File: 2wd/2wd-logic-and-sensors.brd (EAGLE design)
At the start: 100 x 80 mm, 12 parts, among them IC1 REG1118

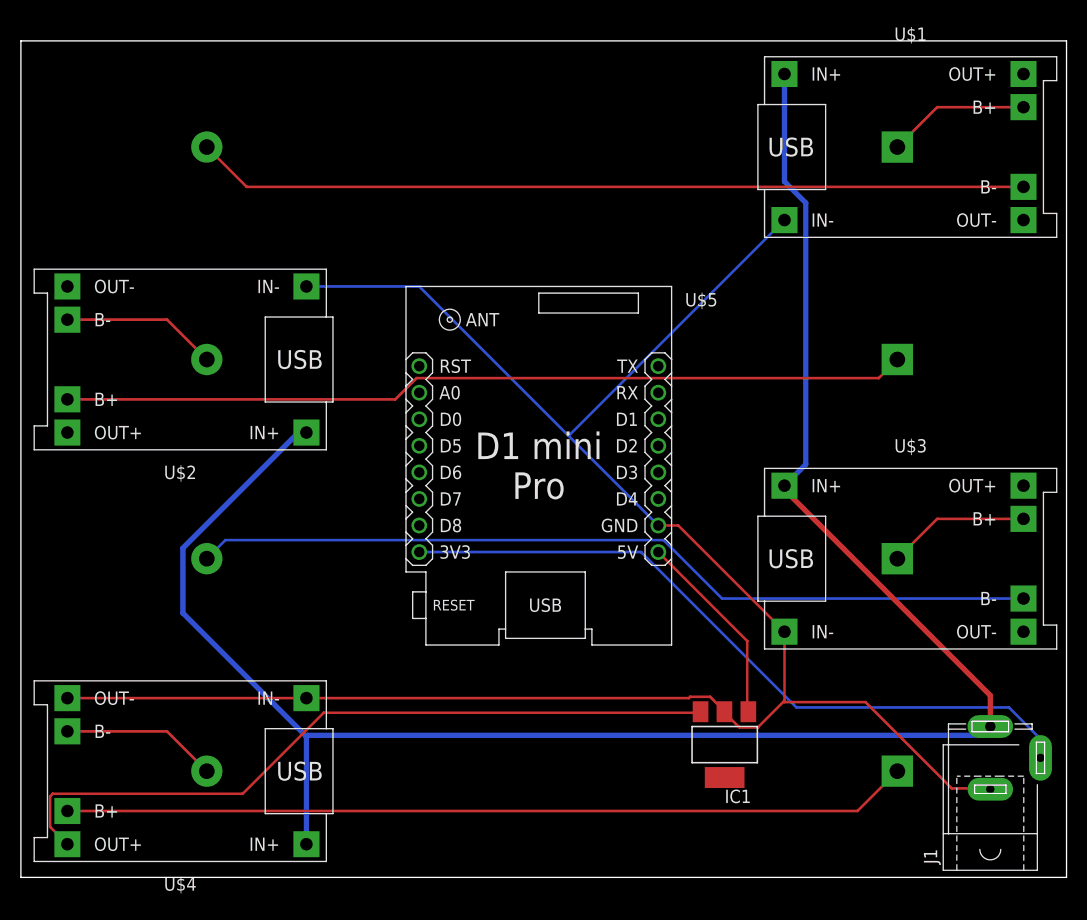
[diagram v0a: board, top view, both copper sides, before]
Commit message: Created two boards in Eagle.
Finally decided to create two boards within one Eagle project.  A motherboard and a power management/motor controller daughterboard.
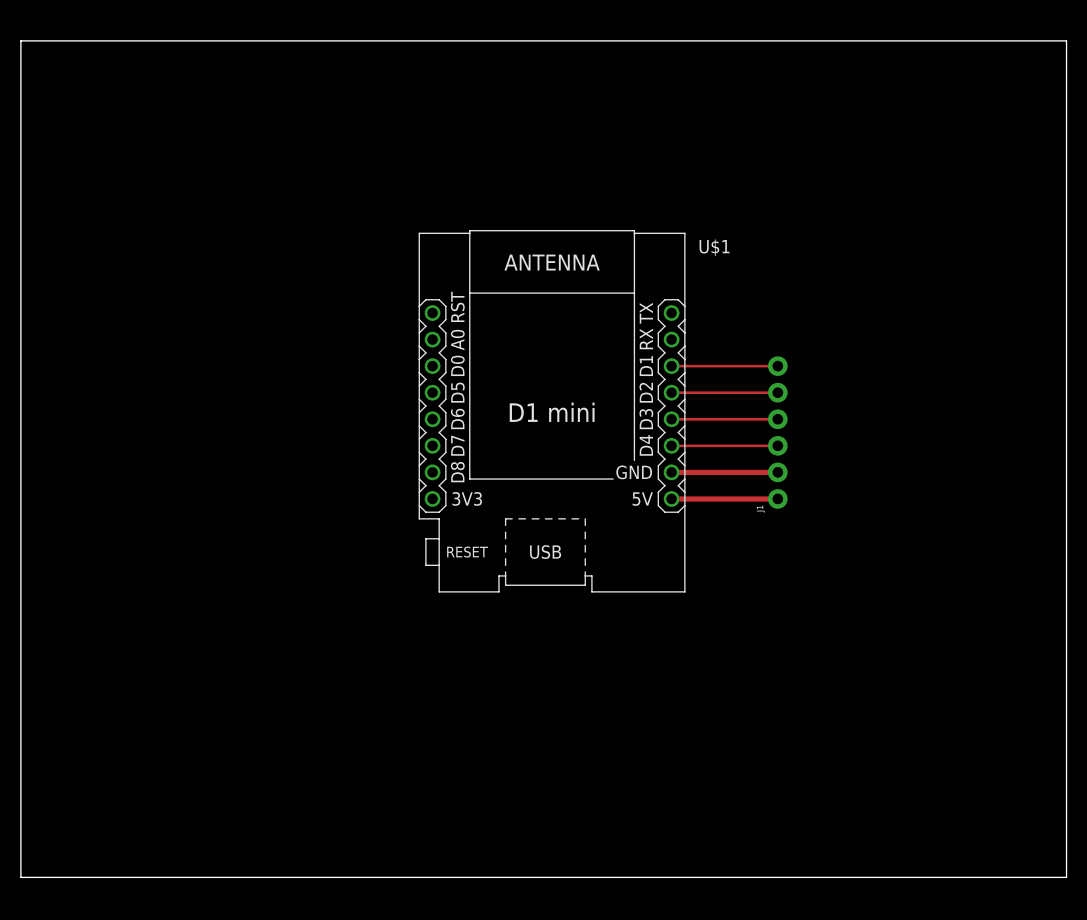
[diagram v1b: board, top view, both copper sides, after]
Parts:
- removed IC1: REG1118, burr-brown:SOT223
- removed U$2, U$3, U$4: BATTERY-CHARGER-LI-PROT, diy-modules:BATTERY-CHARGER-LI-PROT
- removed U$5: WEMOS-D1-MINI-PRO, diy-modules:WEMOS-D1-MINI-PRO
- removed U$6, U$7, U$8, U$9: BATTERY-LI-MH12210, diy-modules:BATTERY-LI-MH12210
- J1: device con-jack:SPC4077 -> SparkFun-Connectors:1X06_NO_SILK
- U$1: value BATTERY-CHARGER-LI-PROT -> WEMOS-D1-MINI; device diy-modules:BATTERY-CHARGER-LI-PROT -> diy-modules:WEMOS-D1-MINI
- moved U$1 42.7 mm to (50.8, 44.5)
- moved J1 32.0 mm to (72.4, 36.2)
- moved FRAME1 1.27 mm to (15.2, -10.2)
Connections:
- removed net GND: IC1.2, J1.1, U$1.IN-, U$2.IN-, U$3.IN-, U$4.IN-, U$4.OUT-, U$5.JP2.7
- removed net N$10: IC1.1, U$5.JP2.8
- removed net N$11: J1.2, U$5.JP1.8
- removed net N$7: U$1.B+, U$9.BAT+
- removed net N$8: U$4.B+, U$6.BAT+
- removed net N$9: IC1.3, U$4.OUT+
- removed net VCC: J1.3, U$1.IN+, U$2.IN+, U$3.IN+, U$4.IN+
- new net 3V3: U$1.JP1.8
- net N$1: now also J1.1, U$1.JP2.8; no longer U$1.B-, U$9.BAT-
- net N$2: now also J1.2, U$1.JP2.7; no longer U$2.B-, U$8.BAT-
- net N$3: now also J1.3, U$1.JP2.6; no longer U$3.B-, U$7.BAT-
- net N$4: now also J1.4, U$1.JP2.5; no longer U$4.B-, U$6.BAT-
- net N$5: now also J1.5, U$1.JP2.4; no longer U$3.B+, U$7.BAT+
- net N$6: now also J1.6, U$1.JP2.3; no longer U$2.B+, U$8.BAT+
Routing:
- net GND: track 189.4 -> 0.00 mm
- net VCC: track 187.7 -> 0.00 mm
- net N$8: track 81.0 -> 0.00 mm
- net N$3: track 81.2 -> 10.2 mm
- net N$9: track 70.8 -> 0.00 mm
- net N$6: track 81.0 -> 10.2 mm
- net N$1: track 79.7 -> 10.2 mm
- net N$11: track 68.7 -> 0.00 mm
- net N$10: track 18.9 -> 0.00 mm
- net N$7: track 13.6 -> 0.00 mm
- net N$4: track 14.9 -> 10.2 mm
- net N$2: track 14.9 -> 10.2 mm
- net N$5: track 13.6 -> 10.2 mm
